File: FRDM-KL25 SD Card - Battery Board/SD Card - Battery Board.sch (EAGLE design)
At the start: 64 parts, among them J3 SSW-108-02-S-D, J4 SSW-110-02-S-D, J5 SSW-108-02-S-D, J6 SSW-106-02-S-D, U1 TPS63001, U2 TPS63002, U3 BQ27510DRZT-G3, U4 BQ24210DQCT

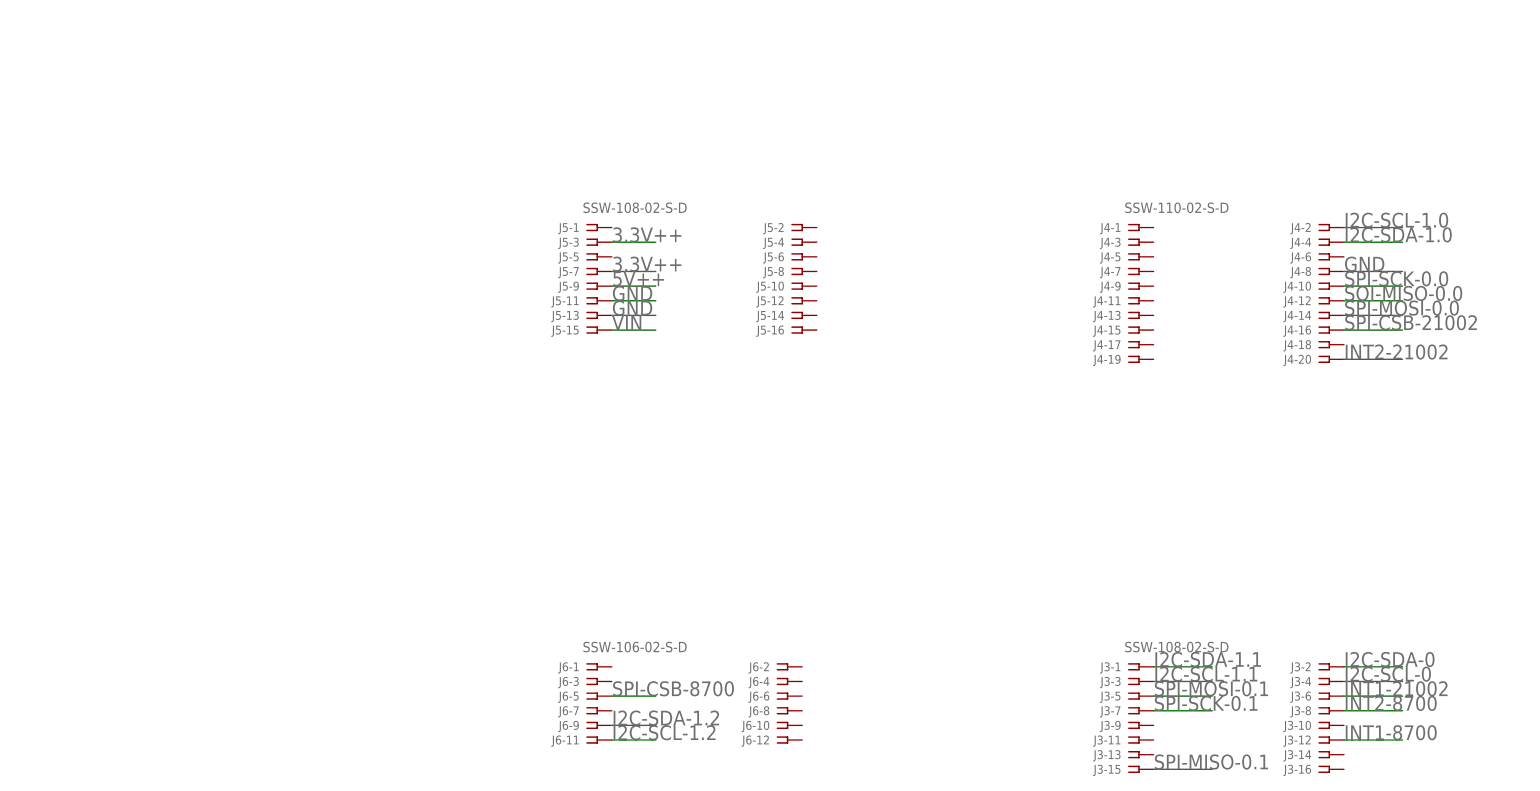
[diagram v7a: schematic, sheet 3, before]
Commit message: FRDM-KL25Z: Fixed baord outline to matxh with Freescales coordinate system. Placed connectors as per Freescales placement file and replaced all previous components on board in the correct orientation. On the schematics the USB connetor was moved from sheet 2 to sheet 3 with all the other connectors.
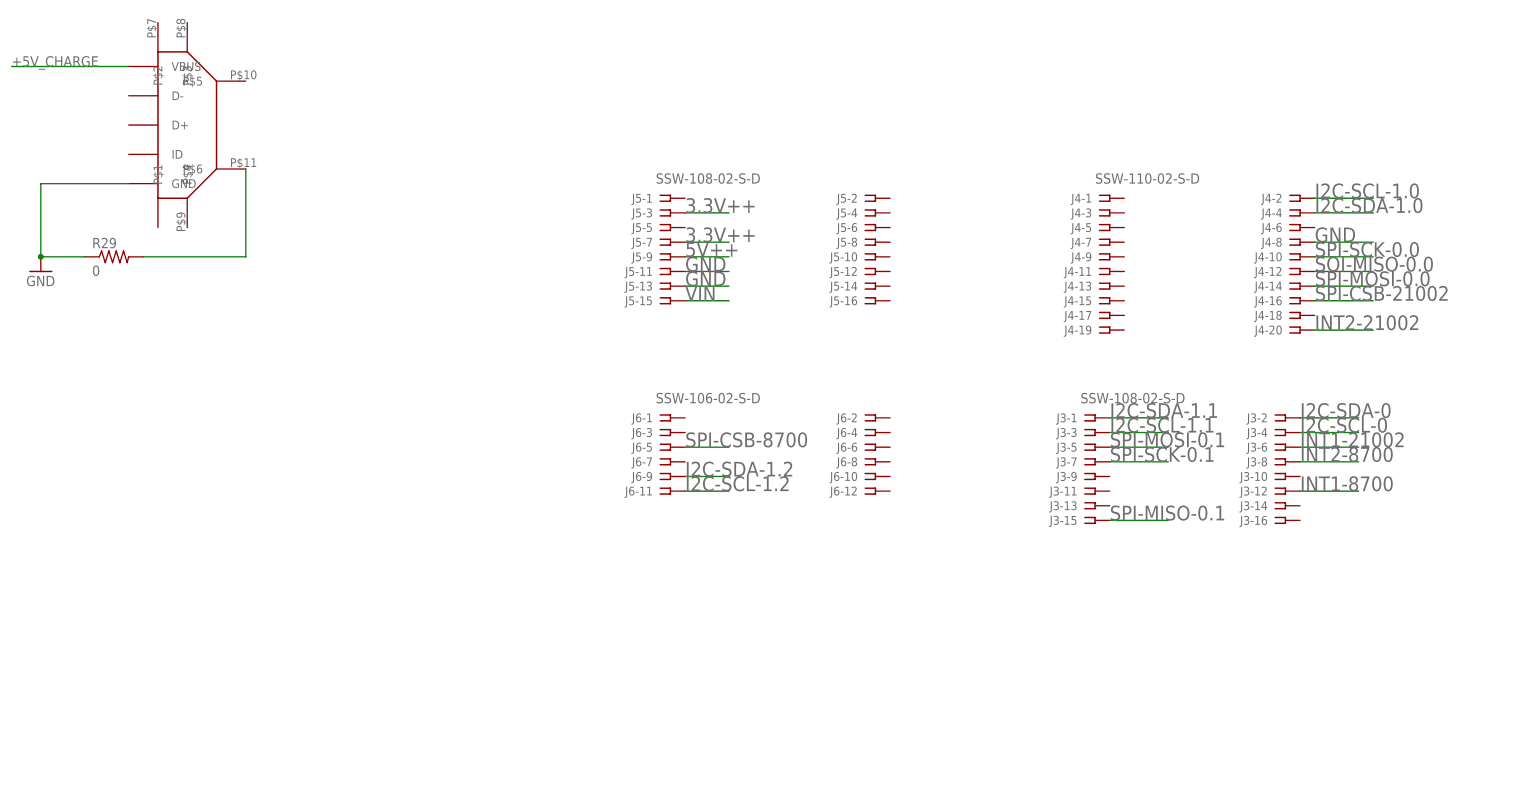
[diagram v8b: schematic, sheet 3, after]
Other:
- moved on the sheet: J3-1, J3-10, J3-11, J3-12, J3-13, J3-14, J3-15, J3-16, J3-2, J3-3, J3-4, J3-5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
